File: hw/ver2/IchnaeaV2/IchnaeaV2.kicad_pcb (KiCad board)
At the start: 4 copper layers, 100 x 100 mm, 144 parts, among them J1 Screw_Terminal_01x09, J2 Screw_Terminal_01x09, J3 Screw_Terminal_01x09, Q1 BSS138, Q10 MCAC80N10Y, Q11 MCAC80N10Y, Q12 MCAC80N10Y, Q13 MCAC80N10Y, Q14 MCAC80N10Y, Q15 MCAC80N10Y, Q16 MCAC80N10Y, Q17 MCAC80N10Y, Q18 MCAC80N10Y, Q19 MCAC80N10Y, Q2 MCAC80N10Y, Q20 MCAC80N10Y, Q21 MCAC80N10Y, Q22 MCAC80N10Y, Q23 MCAC80N10Y, Q24 MCAC80N10Y, Q25 MCAC80N10Y, Q3 MCAC80N10Y, Q4 MCAC80N10Y, Q5 MCAC80N10Y, Q6 MCAC80N10Y, Q7 MCAC80N10Y, Q8 MCAC80N10Y, Q9 MCAC80N10Y, U1 LTC7871, U2 HIP2210, U3 HIP2210, U4 HIP2210, U5 HIP2210, U6 HIP2210, U7 HIP2210

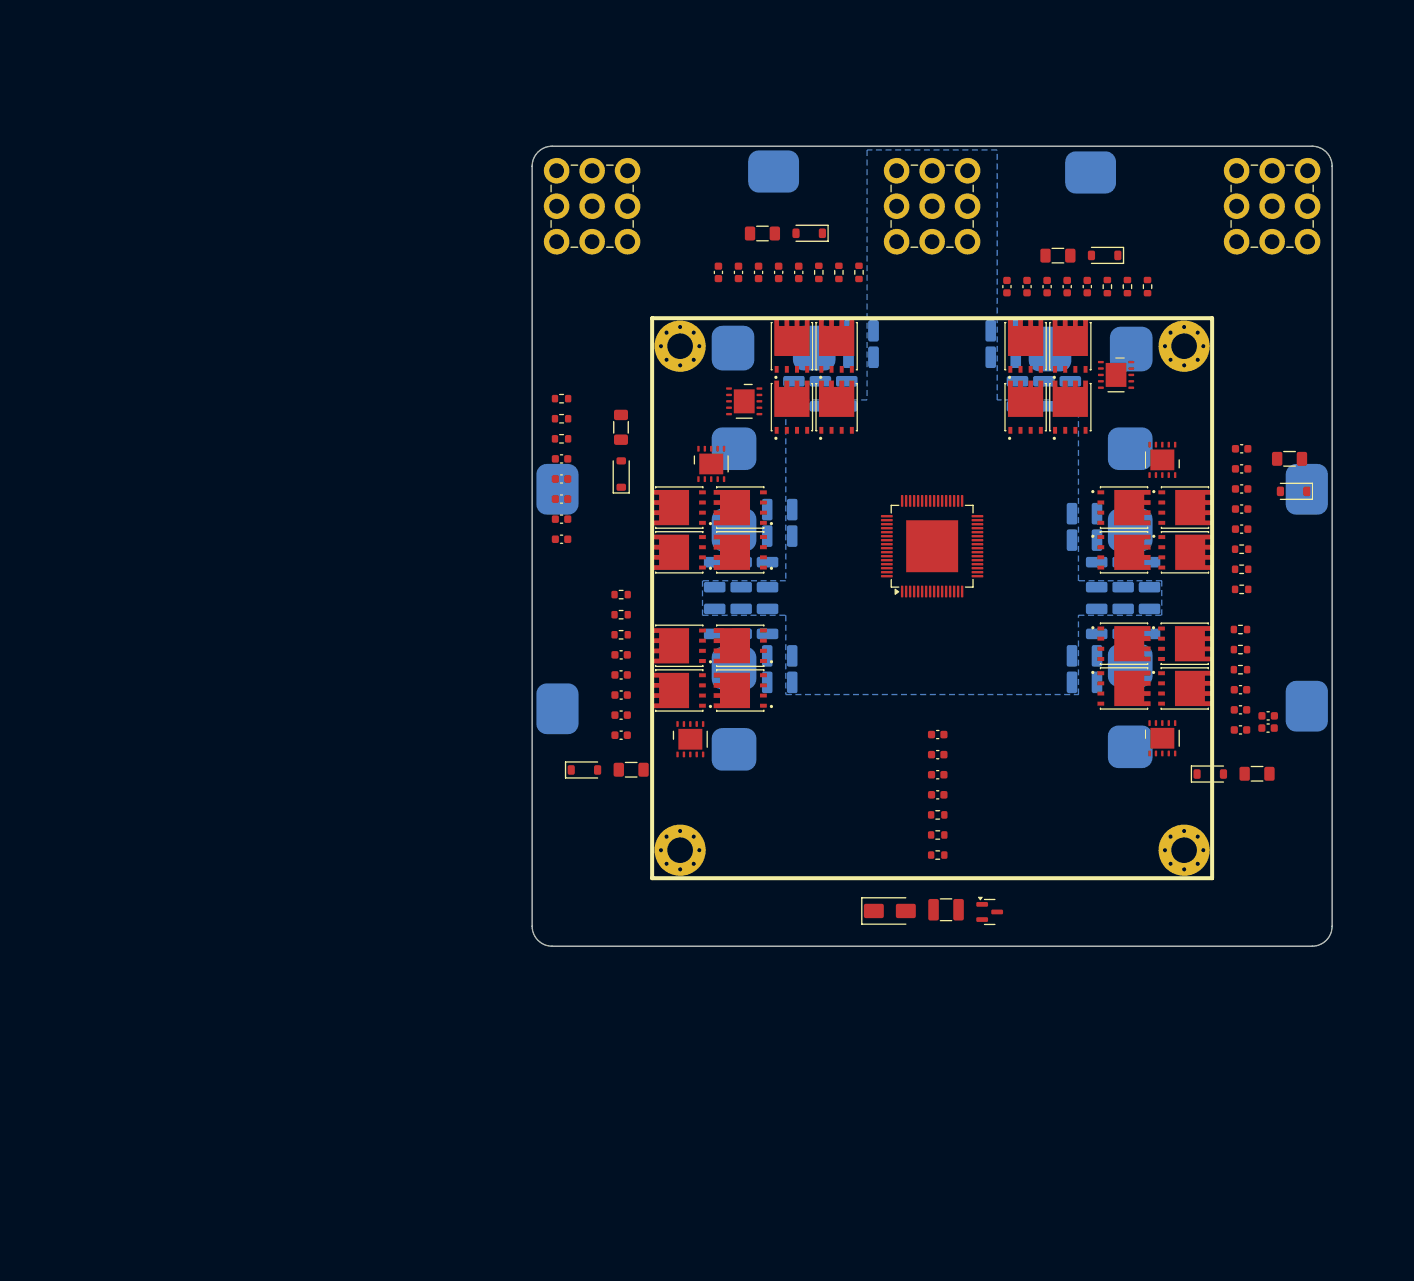
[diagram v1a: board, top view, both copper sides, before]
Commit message: Trying to further compress power loop area
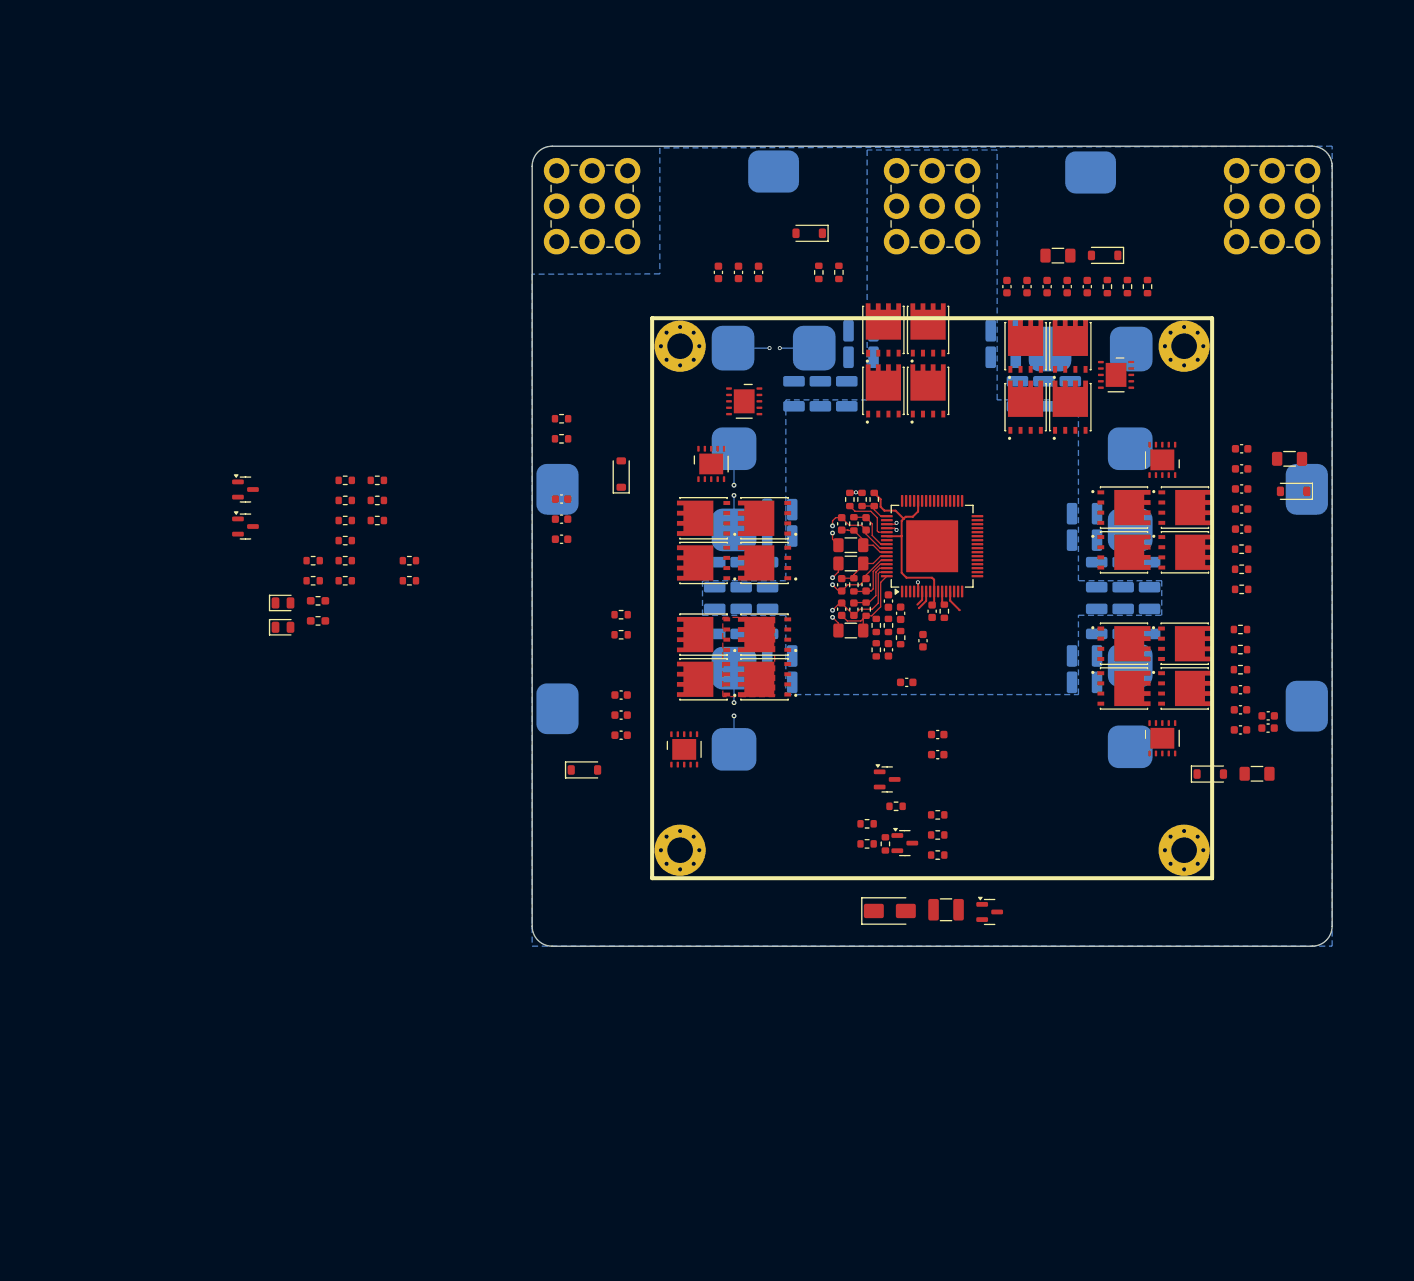
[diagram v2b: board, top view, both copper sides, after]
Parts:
- removed C4: 100nF, Capacitor_SMD:C_0603_1608Metric
- added C66: 100nF, Capacitor_SMD:C_0603_1608Metric, F.Cu at (139.5, 111.9)
- added C67: 47pF, Capacitor_SMD:C_0603_1608Metric, F.Cu at (141.8, 122.0)
- added C68: 47pF, Capacitor_SMD:C_0603_1608Metric, F.Cu at (139.5, 118.0)
- added C69: 100nF, Capacitor_SMD:C_0603_1608Metric, F.Cu at (143.9, 116.8)
- added C70: 100nF, Capacitor_SMD:C_0603_1608Metric, F.Cu at (141.1, 113.4)
- added D8: Yellow LED, LED_SMD:LED_0805_2012Metric, F.Cu at (63.9, 112.1)
- added D9: Yellow LED, LED_SMD:LED_0805_2012Metric, F.Cu at (63.9, 115.1)
- added Q26: BSS138, Package_TO_SOT_SMD:SOT-23, F.Cu at (59.2, 97.9)
- added Q27: BSS84, Package_TO_SOT_SMD:SOT-23, F.Cu at (59.2, 102.5)
- added Q28: BSS138, Package_TO_SOT_SMD:SOT-23, F.Cu at (139.4, 134.2)
- added Q29: BSS138, Package_TO_SOT_SMD:SOT-23, F.Cu at (141.6, 142.1)
- added R28: 22k, Resistor_SMD:R_0603_1608Metric, F.Cu at (146.5, 113.1)
- added R29: 10k, Resistor_SMD:R_0603_1608Metric, F.Cu at (137.8, 99.2)
- added R30: 30k, Resistor_SMD:R_0603_1608Metric, F.Cu at (136.2, 99.2)
- added R31: 470k, Resistor_SMD:R_0603_1608Metric, F.Cu at (138.0, 114.9)
- added R32: 15k, Resistor_SMD:R_0603_1608Metric, F.Cu at (138.0, 118.0)
- added R33: 787k, Resistor_SMD:R_0603_1608Metric_Pad0.98x0.95mm_HandSolder, F.Cu at (68.2, 111.8)
- added R34: 120k, Resistor_SMD:R_0603_1608Metric, F.Cu at (67.6, 106.8)
- added R35: 470k, Resistor_SMD:R_0603_1608Metric, F.Cu at (67.6, 109.3)
- added R36: 10k, Resistor_SMD:R_0603_1608Metric, F.Cu at (71.6, 96.8)
- added R37: 10k, Resistor_SMD:R_0603_1608Metric, F.Cu at (71.6, 99.3)
- added R38: 10k, Resistor_SMD:R_0603_1608Metric, F.Cu at (71.6, 101.8)
- added R39: 787k, Resistor_SMD:R_0603_1608Metric_Pad0.98x0.95mm_HandSolder, F.Cu at (68.2, 114.3)
- added R40: 10k, Resistor_SMD:R_0603_1608Metric, F.Cu at (71.6, 104.3)
- added R41: 100, Resistor_SMD:R_0603_1608Metric, F.Cu at (71.6, 106.8)
- added R42: 100, Resistor_SMD:R_0603_1608Metric, F.Cu at (71.6, 109.3)
- added R43: 10k, Resistor_SMD:R_0603_1608Metric, F.Cu at (75.6, 96.8)
- added R44: 10k, Resistor_SMD:R_0603_1608Metric, F.Cu at (75.6, 99.3)
- added R45: 10k, Resistor_SMD:R_0603_1608Metric, F.Cu at (75.6, 101.8)
- added R46: 10k, Resistor_SMD:R_0603_1608Metric, F.Cu at (140.5, 137.5)
- added R47: 3k, Resistor_SMD:R_0603_1608Metric, F.Cu at (141.1, 116.4)
- added R48: 1k, Resistor_SMD:R_0603_1608Metric, F.Cu at (139.5, 114.9)
- added R49: 100, Resistor_SMD:R_0603_1608Metric, F.Cu at (136.9, 139.7)
- added R50: 10k, Resistor_SMD:R_0603_1608Metric, F.Cu at (136.9, 142.2)
- added R51: 10k, Resistor_SMD:R_0603_1608Metric, F.Cu at (139.2, 142.2)
- added R52: 68k, Resistor_SMD:R_0603_1608Metric, F.Cu at (134.7, 99.2)
- added R53: 10k, Resistor_SMD:R_0603_1608Metric, F.Cu at (79.7, 106.8)
- added R55: 10k, Resistor_SMD:R_0603_1608Metric, F.Cu at (79.7, 109.3)
- moved R23 43.3 mm to (135.2, 109.8), turned to 90 degrees
- moved C34 41.2 mm to (136.7, 109.8), turned to -90 degrees
- moved R18 40.5 mm to (134.8, 104.9), turned to 0 degrees
- moved C33 37.4 mm to (133.7, 109.8), turned to 90 degrees
- moved R22 33.4 mm to (134.8, 107.2), turned to 0 degrees
- moved C28 32.5 mm to (136.7, 102.2)
- moved R26 32.5 mm to (134.8, 115.5)
- moved C27 32.4 mm to (133.7, 102.2), turned to -90 degrees
- moved R19 31.4 mm to (135.2, 102.2), turned to -90 degrees
- moved R27 30.7 mm to (136.7, 112.9), turned to -90 degrees
- moved C40 29.7 mm to (135.2, 112.9), turned to 90 degrees
- moved C39 28.8 mm to (133.7, 112.9), turned to -90 degrees
- moved C3 20.5 mm to (145.0, 113.1), turned to -90 degrees
- moved Q15 11.6 mm to (138.9, 85.6)
- moved Q16 11.6 mm to (138.9, 78.0)
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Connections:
- C12 pad 1: +VSW -> VHIGH
- C13 pad 1: +VSW -> VHIGH
- C18 pad 1: +VSW -> VHIGH
- C19 pad 1: +VSW -> VHIGH
- C24 pad 1: +VSW -> VHIGH
- C25 pad 1: +VSW -> VHIGH
- C30 pad 1: +VSW -> VHIGH
- C31 pad 1: +VSW -> VHIGH
- C36 pad 1: +VSW -> VHIGH
- C37 pad 1: +VSW -> VHIGH
- C6 pad 1: +VSW -> VHIGH
- C7 pad 1: +VSW -> VHIGH
- J1 pad 1: +VHIGH -> VHIGH
- J1 pad 2: +VHIGH -> VHIGH
- J1 pad 3: +VHIGH -> VHIGH
- J1 pad 4: +VHIGH -> VHIGH
- J1 pad 5: +VHIGH -> VHIGH
- J1 pad 6: +VHIGH -> VHIGH
- J1 pad 7: +VHIGH -> VHIGH
- J1 pad 8: +VHIGH -> VHIGH
- J1 pad 9: +VHIGH -> VHIGH
- J2 pad 1: +VLOW -> VLOW
- J2 pad 2: +VLOW -> VLOW
- J2 pad 3: +VLOW -> VLOW
- J2 pad 4: +VLOW -> VLOW
- J2 pad 5: +VLOW -> VLOW
- J2 pad 6: +VLOW -> VLOW
- J2 pad 7: +VLOW -> VLOW
- J2 pad 8: +VLOW -> VLOW
- J2 pad 9: +VLOW -> VLOW
- Q1 pad 2: GNDD -> GND
- Q10 pad 1: +VSW -> VHIGH
- Q12 pad 1: +VSW -> VHIGH
- Q14 pad 1: +VSW -> VHIGH
- Q16 pad 1: +VSW -> VHIGH
- Q18 pad 1: +VSW -> VHIGH
- Q2 pad 1: +VSW -> VHIGH
- Q20 pad 1: +VSW -> VHIGH
- Q22 pad 1: +VSW -> VHIGH
- Q24 pad 1: +VSW -> VHIGH
- Q4 pad 1: +VSW -> VHIGH
- Q6 pad 1: +VSW -> VHIGH
- Q8 pad 1: +VSW -> VHIGH
- R12 pad 2: +VSW -> VHIGH
- R16 pad 2: +VSW -> VHIGH
- R2 pad 1: GNDD -> GND
- R20 pad 2: +VSW -> VHIGH
- R24 pad 2: +VSW -> VHIGH
- R4 pad 2: +VSW -> VHIGH
- R8 pad 2: +VSW -> VHIGH
- U1 pad 1: unconnected-(U1-SS-Pad1) -> LTC_SS
- U1 pad 10: unconnected-(U1-IMON-Pad10) -> LTC_IMON
- U1 pad 11: unconnected-(U1-SETCUR-Pad11) -> LTC_SETCUR
- U1 pad 13: unconnected-(U1-OVHigh-Pad13) -> LTC_OV_HIGH
- U1 pad 14: unconnected-(U1-UVHigh-Pad14) -> LTC_UV_HIGH
- U1 pad 15: unconnected-(U1-OVLow-Pad15) -> LTC_OV_LOW
- U1 pad 16: unconnected-(U1-SGND-Pad16) -> GND
- U1 pad 27: unconnected-(U1-RUN-Pad27) -> LTC_RUN
- U1 pad 3: unconnected-(U1-VFBLow-Pad3) -> LTC_VFB_LOW
- U1 pad 30: unconnected-(U1-PGOOD-Pad30) -> PGOOD
- U1 pad 35: unconnected-(U1-FAULT-Pad35) -> FAULT
- U1 pad 37: unconnected-(U1-CSB-Pad37) -> /PowerStage/IO_LTC_CSB
- U1 pad 38: unconnected-(U1-SDO-Pad38) -> /PowerStage/IO_LTC_SDO
- U1 pad 39: unconnected-(U1-SDI-Pad39) -> /PowerStage/IO_LTC_SDI
- U1 pad 4: unconnected-(U1-ITHLow-Pad4) -> LTC_ITH_LOW
- U1 pad 40: unconnected-(U1-SCLK-Pad40) -> /PowerStage/IO_LTC_SCK
- U1 pad 44: unconnected-(U1-DRVSET-Pad44) -> +5P
- U1 pad 45: unconnected-(U1-SGND-Pad45) -> GND
- U1 pad 48: +VSW -> VHIGH
- U1 pad 49: unconnected-(U1-ILM-Pad49) -> LTC_ILIM
- U1 pad 5: unconnected-(U1-SGND-Pad5) -> GND
- U1 pad 51: unconnected-(U1-MODE-Pad51) -> LTC_MODE
- U1 pad 52: unconnected-(U1-SYNC-Pad52) -> LTC_SYNC
- U1 pad 53: unconnected-(U1-FREQ-Pad53) -> LTC_FREQ
- U1 pad 54: unconnected-(U1-BUCK-Pad54) -> +5P
- U1 pad 6: unconnected-(U1-ITHHigh-Pad6) -> LTC_ITH_HIGH
- U1 pad 65: unconnected-(U1-SGND-Pad65) -> GND
- U1 pad 7: unconnected-(U1-VFBHigh-Pad7) -> LTC_FB_HIGH
- U2 pad 1: +VSW -> VHIGH
- U3 pad 1: +VSW -> VHIGH
- U4 pad 1: +VSW -> VHIGH
- U5 pad 1: +VSW -> VHIGH
- U6 pad 1: +VSW -> VHIGH
- U7 pad 1: +VSW -> VHIGH
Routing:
- net VLOW: track 0.00 -> 114.7 mm, vias 0 -> 6
- net Net-(Q14-S): track 0.00 -> 33.3 mm, vias 0 -> 2
- net Net-(Q22-S): track 0.00 -> 30.1 mm, vias 0 -> 2
- net Net-(Q18-S): track 0.00 -> 27.3 mm, vias 0 -> 2
- net +5P: track 0.00 -> 25.5 mm
- net /PowerStage/Phase6/SNSA+: track 0.00 -> 12.0 mm
- net /PowerStage/Phase6/SNSD+: track 0.00 -> 7.64 mm
- net /PowerStage/Phase5/SNSA+: track 0.00 -> 7.19 mm
- net /PowerStage/Phase4/SNSA+: track 0.00 -> 7.18 mm
- net /PowerStage/Phase5/SNSD+: track 0.00 -> 7.06 mm
- net LTC_FREQ: track 0.00 -> 6.94 mm
- net /PowerStage/Phase4/SNSD+: track 0.00 -> 6.37 mm
- net LTC_ILIM: track 0.00 -> 3.89 mm
- net LTC_OV_HIGH: track 0.00 -> 2.83 mm
- net GND: track 0.00 -> 2.74 mm, vias 0 -> 2
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- added copper zone on In1.Cu, net GND
- added copper zone on F.Cu, net Net-(Q22-S)
- added copper zone on B.Cu, net VLOW

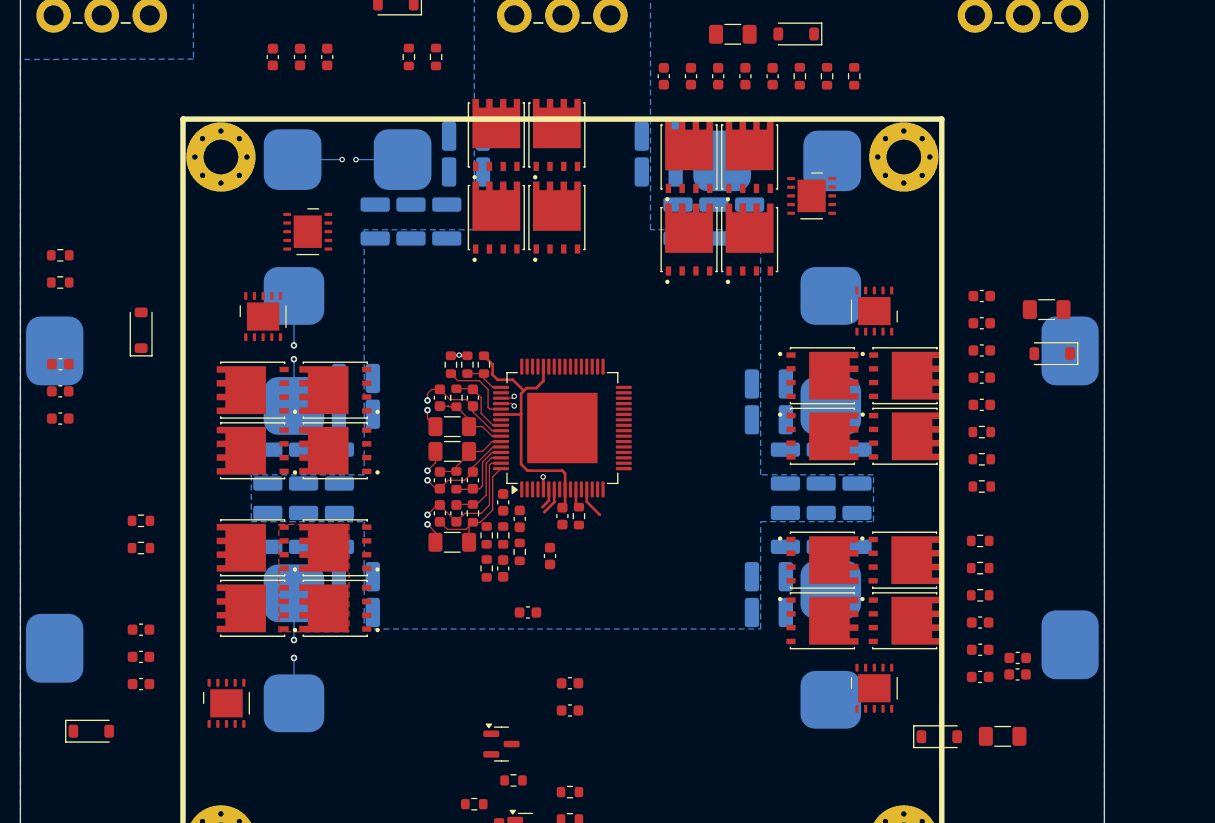
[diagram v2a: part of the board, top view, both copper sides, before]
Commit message: Not quite happy with the power stage just yet.
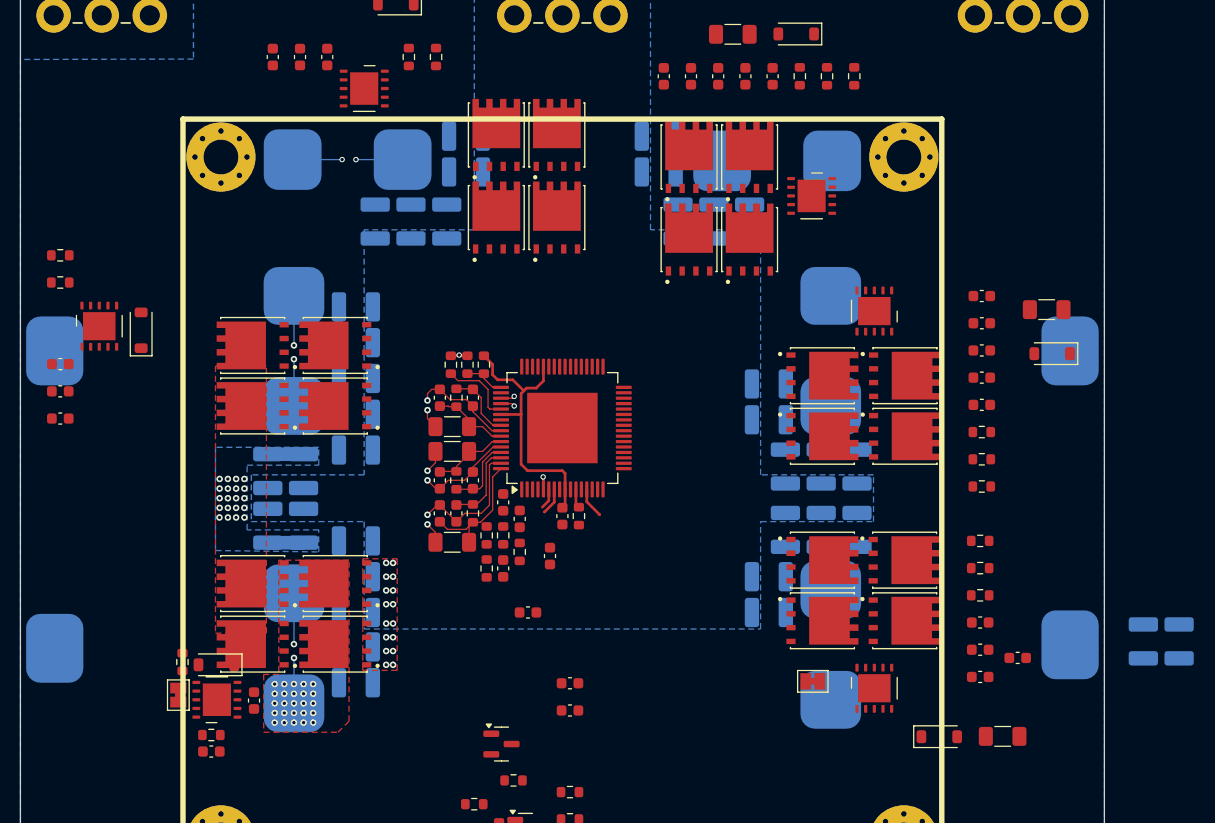
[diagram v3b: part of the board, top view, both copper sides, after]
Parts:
- added C4: 10uF-100v, Capacitor_SMD:C_1210_3225Metric_Pad1.33x2.70mm_HandSolder, B.Cu at (201.9, 124.7)
- added C71: 10uF-100v, Capacitor_SMD:C_1210_3225Metric_Pad1.33x2.70mm_HandSolder, B.Cu at (198.6, 124.7)
- added C72: 10uF-100v, Capacitor_SMD:C_1210_3225Metric_Pad1.33x2.70mm_HandSolder, B.Cu at (117.8, 109.0)
- added C73: 10uF-100v, Capacitor_SMD:C_1210_3225Metric_Pad1.33x2.70mm_HandSolder, B.Cu at (121.1, 109.0)
- added JP1: SolderJumper_2_Bridged, Jumper:SolderJumper-2_P1.3mm_Bridged_Pad1.0x1.5mm, F.Cu at (168.1, 128.4)
- added JP2: SolderJumper_2_Bridged, Jumper:SolderJumper-2_P1.3mm_Bridged_Pad1.0x1.5mm, F.Cu at (109.6, 129.6)
- C1, C3: value 10uF -> 10uF-25V
- C11, C17, C23, C29, C35, C41, C42, C43, C44, C45, C46, C47, C48, C49, C50, C51, C52, C53, C54, C55, C56, C57, C58, C59, C60, C61, C62, C63, C64, C65: value 10uF -> 10uF-100v
- C12, C18, C24, C30, C36, C6: value 4.7uF -> 10uF-25V
- C37, C7: value 100nF -> 10uF-100v; footprint Capacitor_SMD:C_0603_1608Metric -> Capacitor_SMD:C_1210_3225Metric_Pad1.33x2.70mm_HandSolder; moved to B.Cu
- C5: value 10uF-75V -> 10uF-100v
- D2, D3, D4, D5, D6, D7: value Z3V3 -> Z5V1
- moved C7 70.5 mm to (117.8, 114.0), turned to 90 degrees
- moved C37 19.3 mm to (121.1, 114.0), turned to 90 degrees
- moved R24 18.4 mm to (112.6, 133.3), turned to 0 degrees
- moved C46 15.5 mm to (126.0, 93.8), turned to 0 degrees
- moved U6 15.1 mm to (102.3, 95.6)
- moved C41 14.9 mm to (126.0, 128.5), turned to 0 degrees
- moved U5 14.2 mm to (126.7, 73.7)
- moved C35 14.0 mm to (126.0, 97.1), turned to 0 degrees
- moved R25 13.6 mm to (109.9, 126.6), turned to -90 degrees
- moved C65 13.5 mm to (126.0, 125.2), turned to 0 degrees
- moved D7 13.1 mm to (113.1, 126.8), turned to 180 degrees
- moved C38 12.3 mm to (116.6, 130.1), turned to 90 degrees
- moved C36 8.99 mm to (112.6, 134.8)
- moved Q18 4.13 mm to (116.4, 97.4)
- moved Q21 4.13 mm to (124.0, 97.4)
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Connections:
- C12 pad 1: VHIGH -> +VSW
- C13 pad 1: VHIGH -> +VSW
- C18 pad 1: VHIGH -> +VSW
- C19 pad 1: VHIGH -> +VSW
- C24 pad 1: VHIGH -> +VSW
- C25 pad 1: VHIGH -> +VSW
- C30 pad 1: VHIGH -> +VSW
- C31 pad 1: VHIGH -> +VSW
- C36 pad 1: VHIGH -> +VSW
- C6 pad 1: VHIGH -> +VSW
- R12 pad 2: VHIGH -> +VSW
- R16 pad 2: VHIGH -> +VSW
- R20 pad 2: VHIGH -> +VSW
- R24 pad 2: VHIGH -> +VSW
- R4 pad 2: VHIGH -> +VSW
- R8 pad 2: VHIGH -> +VSW
- U2 pad 1: VHIGH -> +VSW
- U2 pad 8: /PowerStage/Phase1/PWM -> Net-(JP1-B)
- U3 pad 1: VHIGH -> +VSW
- U4 pad 1: VHIGH -> +VSW
- U5 pad 1: VHIGH -> +VSW
- U6 pad 1: VHIGH -> +VSW
- U7 pad 1: VHIGH -> +VSW
- U7 pad 8: /PowerStage/Phase6/PWM -> Net-(JP2-B)
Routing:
- net VLOW: track 114.7 -> 106.5 mm
- net VHIGH: track 0.00 -> 6.60 mm, vias 0 -> 20
- net Net-(Q18-S): track 27.3 -> 29.0 mm
- net Net-(Q22-S): track 30.1 -> 28.7 mm, vias 2 -> 27
- net GND: vias 2 -> 18
- added copper zone on F.Cu, net GND
- added copper zone on B.Cu, net VHIGH
- added copper zone on F.Cu, net VHIGH
